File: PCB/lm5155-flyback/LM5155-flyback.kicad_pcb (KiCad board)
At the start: 2 copper layers, 49 x 35.5 mm, 36 parts, among them Q1 DMT6030LFCL-7, T1 EP7-5801_750315825, U1 LM5155

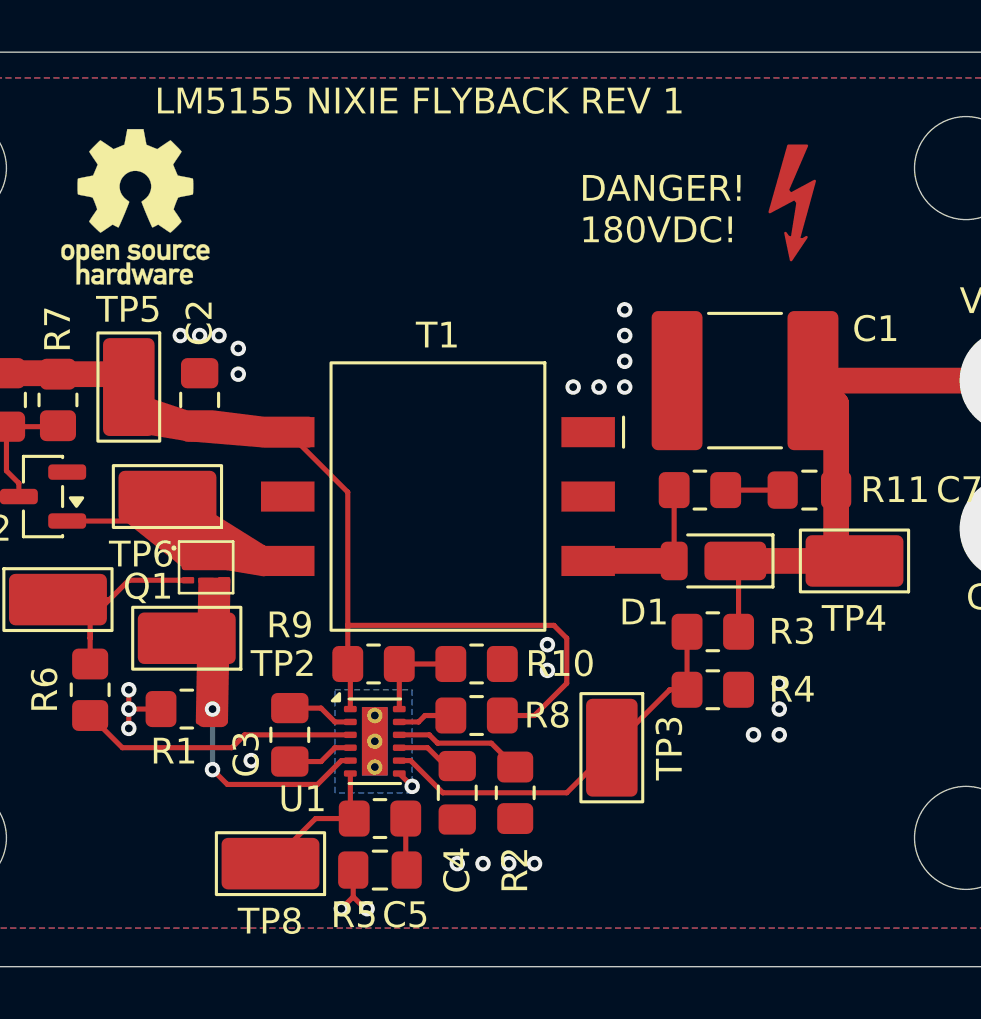
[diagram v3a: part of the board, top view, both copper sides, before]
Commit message: Fix small issue with feedback resistors. Hopefully wont cause real issues with Rev 1
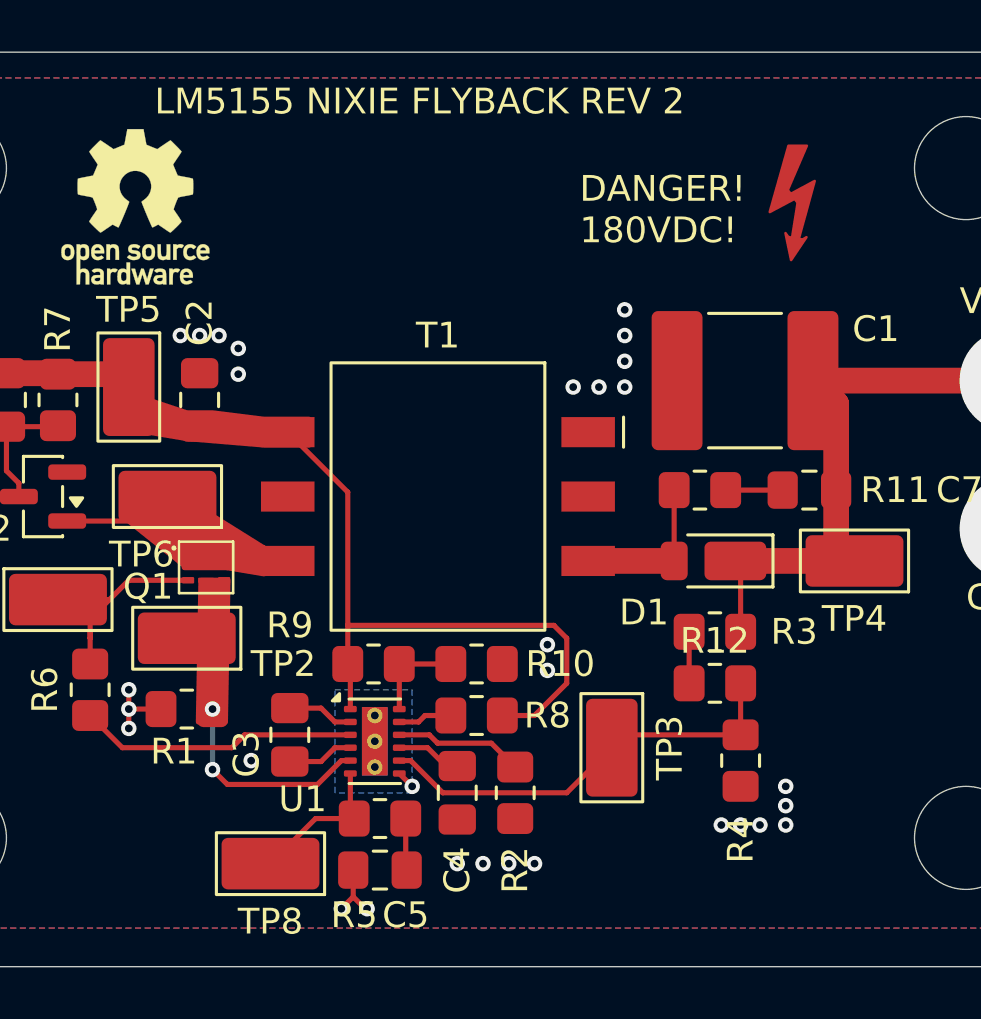
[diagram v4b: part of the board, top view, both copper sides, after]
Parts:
- added R12: 499k, Resistor_SMD:R_0805_2012Metric_Pad1.20x1.40mm_HandSolder, F.Cu at (191.5, 105.2)
- C4: value 30n -> 33n
- R2: value 87.5k -> 88.7k
- R3: value 1Meg -> 499k
- R7: value 3.8k -> 3.79k
- moved R4 2.95 mm to (192.5, 108.2), turned to -90 degrees
- moved R3 0.08 mm to (191.5, 103.2)
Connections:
- net Net-(D1-A) renamed /HV
- R3 pad 2: /FB -> Net-(R12-Pad1)
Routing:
- net Net-(R12-Pad1): track 0.00 -> 2.00 mm
- net /FB: track 15.6 -> 16.7 mm
- net GND: vias 30 -> 32
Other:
- board text added: "LM5155 NIXIE FLYBACK REV 2"
- board text removed: "LM5155 NIXIE FLYBACK REV 1"
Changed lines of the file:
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@@
 	(net 0 "")
 	(net 1 "unconnected-(T1-Pad2)")
-	(net 2 "Net-(D1-A)")
+	(net 2 "/HV")
 	(net 3 "/CS")
 	(net 4 "GND")
@@
 	(net 19 "/VOUT")
 	(net 20 "unconnected-(D2-NC-Pad2)")
+	(net 21 "Net-(R12-Pad1)")
 	(footprint "Symbol:Symbol_HighVoltage_NoTriangle_2x5mm_Copper"
 		(layer "F.Cu")
@@
 			)
 		)
-		(property "Value" "30n"
+		(property "Value" "33n"
 			(at 0 1.68 90)
 			(layer "F.Fab")
@@
 			)
 		)
-		(property "Value" "3.8k"
+		(property "Value" "3.79k"
 			(at 0 1.65 90)
 			(layer "F.Fab")
@@
 			(layers "F.Cu" "F.Mask" "F.Paste")
 			(roundrect_rratio 0.208333)
-			(net 2 "Net-(D1-A)")
+			(net 2 "/HV")
 			(pintype "passive")
 		)
@@
 			)
 		)
-		(property "Value" "87.5k"
+		(property "Value" "88.7k"
 			(at 0 1.65 90)
 			(layer "F.Fab")
@@
 	(footprint "Resistor_SMD:R_0805_2012Metric_Pad1.20x1.40mm_HandSolder"
 		(layer "F.Cu")
-		(at 191.42 103.25 180)
+		(at 191.5 103.25 180)
 		(descr "Resistor SMD 0805 (2012 Metric), square (rectangular) end terminal, IPC-7351 nominal with elongated pad for handsoldering. (Body size source: IPC-SM-782 page 72, https://www.pcb-3d.com/wordpress/wp-content/uploads/ipc-sm-782a_amendment_1_and_2.pdf), generated with kicad-footprint-generator")
 		(tags "resistor handsolder")
@@
 			)
 		)
-		(property "Value" "1Meg"
+		(property "Value" "499k"
 			(at 0 1.65 0)
 			(layer "F.Fab")
@@
 			(layers "F.Cu" "F.Mask" "F.Paste")
 			(roundrect_rratio 0.208333)
-			(net 12 "/FB")
+			(net 21 "Net-(R12-Pad1)")
 			(pintype "passive")
 		)
@@
 			(size 1.17 2.08)
 			(layers "F.Cu" "F.Mask" "F.Paste")
-			(net 2 "Net-(D1-A)")
+			(net 2 "/HV")
 			(pinfunction "3")
 			(pintype "passive")
@@
 	(footprint "Resistor_SMD:R_0805_2012Metric_Pad1.20x1.40mm_HandSolder"
 		(layer "F.Cu")
-		(at 191.42 105.5)
+		(at 192.5 108.25 -90)
 		(descr "Resistor SMD 0805 (2012 Metric), square (rectangular) end terminal, IPC-7351 nominal with elongated pad for handsoldering. (Body size source: IPC-SM-782 page 72, https://www.pcb-3d.com/wordpress/wp-content/uploads/ipc-sm-782a_amendment_1_and_2.pdf), generated with kicad-footprint-generator")
 		(tags "resistor handsolder")
 		(property "Reference" "R4"
-			(at 3.08 0 0)
+			(at 3.08 0 90)
 			(layer "F.SilkS")
 			(effects
@@
 		)
 		(property "Value" "5.6k"
+			(at 0 1.65 90)
+			(layer "F.Fab")
+			(effects
+				(font
+					(size 1 1)
+					(thickness 0.15)
+				)
+			)
+		)
+		(property "Datasheet" "~"
+			(at 0 0 90)
+			(layer "F.Fab")
+			(hide yes)
+			(effects
+				(font
+					(size 1.27 1.27)
+					(thickness 0.15)
+				)
+			)
+		)
+		(property "Description" "Resistor"
+			(at 0 0 90)
+			(layer "F.Fab")
+			(hide yes)
+			(effects
+				(font
+					(size 1.27 1.27)
+					(thickness 0.15)
+				)
+			)
+		)
+		(property ki_fp_filters "R_*")
+		(sheetname "/")
+		(sheetfile "LM5155-flyback.kicad_sch")
+		(attr smd)
+		(fp_line
+			(start -0.227064 0.735)
+			(end 0.227064 0.735)
+			(stroke
+				(width 0.12)
+				(type solid)
+			)
+			(layer "F.SilkS")
+		)
+		(fp_line
+			(start -0.227064 -0.735)
+			(end 0.227064 -0.735)
+			(stroke
+				(width 0.12)
+				(type solid)
+			)
+			(layer "F.SilkS")
+		)
+		(fp_rect
+			(start -1.85 -0.95)
+			(end 1.85 0.95)
+			(stroke
+				(width 0.05)
+				(type solid)
+			)
+			(fill no)
+			(layer "F.CrtYd")
+		)
+		(fp_rect
+			(start -1 -0.625)
+			(end 1 0.625)
+			(stroke
+				(width 0.1)
+				(type solid)
+			)
+			(fill no)
+			(layer "F.Fab")
+		)
+		(fp_text user "${REFERENCE}"
+			(at 0 0 90)
+			(layer "F.Fab")
+			(effects
+				(font
+					(size 0.5 0.5)
+					(thickness 0.08)
+				)
+			)
+		)
+		(pad "1" smd roundrect
+			(at -1 0 270)
+			(size 1.2 1.4)
+			(layers "F.Cu" "F.Mask" "F.Paste")
+			(roundrect_rratio 0.208333)
+			(net 12 "/FB")
+			(pintype "passive")
+		)
+		(pad "2" smd roundrect
+			(at 1 0 270)
+			(size 1.2 1.4)
+			(layers "F.Cu" "F.Mask" "F.Paste")
+			(roundrect_rratio 0.208333)
+			(net 4 "GND")
+			(pintype "passive")
+		)
+		(embedded_fonts no)
+		(model "${KICAD9_3DMODEL_DIR}/Resistor_SMD.3dshapes/R_0805_2012Metric.step"
+			(offset
+				(xyz 0 0 0)
+			)
+			(scale
+				(xyz 1 1 1)
+			)
+			(rotate
+				(xyz 0 0 0)
+			)
+		)
+	)
+	(footprint "Resistor_SMD:R_0805_2012Metric_Pad1.20x1.40mm_HandSolder"
+		(layer "F.Cu")
+		(at 191.5 105.25)
+		(descr "Resistor SMD 0805 (2012 Metric), square (rectangular) end terminal, IPC-7351 nominal with elongated pad for handsoldering. (Body size source: IPC-SM-782 page 72, https://www.pcb-3d.com/wordpress/wp-content/uploads/ipc-sm-782a_amendment_1_and_2.pdf), generated with kicad-footprint-generator")
+		(tags "resistor handsolder")
+		(property "Reference" "R12"
+			(at 0 -1.65 0)
+			(layer "F.SilkS")
+			(effects
+				(font
+					(size 1 1)
+					(thickness 0.15)
+				)
+			)
+		)
+		(property "Value" "499k"
 			(at 0 1.65 0)
 			(layer "F.Fab")
@@
 			(layers "F.Cu" "F.Mask" "F.Paste")
 			(roundrect_rratio 0.208333)
-			(net 12 "/FB")
+			(net 21 "Net-(R12-Pad1)")
 			(pintype "passive")
 		)
@@
 			(layers "F.Cu" "F.Mask" "F.Paste")
 			(roundrect_rratio 0.208333)
-			(net 4 "GND")
+			(net 12 "/FB")
 			(pintype "passive")
 		)
@@
 			(layers "F.Cu" "F.Mask" "F.Paste")
 			(roundrect_rratio 0.2380952381)
-			(net 2 "Net-(D1-A)")
+			(net 2 "/HV")
 			(pinfunction "A")
 			(pintype "passive")
@@
 		)
 	)
-	(gr_text "LM5155 NIXIE FLYBACK REV 1"
+	(gr_text "LM5155 NIXIE FLYBACK REV 2"
 		(at 169.75 83.25 0)
 		(layer "F.SilkS")
@@
 	)
 	(via
+		(at 191.75 110.75)
+		(size 0.6)
+		(drill 0.3)
+		(layers "F.Cu" "B.Cu")
+		(free yes)
+		(net 4)
+	)
+	(via
 		(at 170.75 91.75)
 		(size 0.6)
@@
 	)
 	(via
+		(at 194.25 109.25)
+		(size 0.6)
+		(drill 0.3)
+		(layers "F.Cu" "B.Cu")
+		(free yes)
+		(net 4)
+	)
+	(via
 		(at 188 90.75)
 		(size 0.6)
@@
 	)
 	(via
-		(at 194 105.25)
+		(at 193.25 110.75)
 		(size 0.6)
 		(drill 0.3)
@@
 	)
 	(via
-		(at 194 107.25)
+		(at 194.25 110.75)
 		(size 0.6)
 		(drill 0.3)
@@
 	)
 	(via
+		(at 194.25 110)
+		(size 0.6)
+		(drill 0.3)
+		(layers "F.Cu" "B.Cu")
+		(free yes)
+		(net 4)
+	)
+	(via
 		(at 184.5 112.25)
 		(size 0.6)
@@
 	)
 	(via
-		(at 173.5 108.25)
+		(at 192.5 110.75)
 		(size 0.6)
 		(drill 0.3)
@@
 	)
 	(via
-		(at 177 114)
+		(at 173.5 108.25)
 		(size 0.6)
 		(drill 0.3)
@@
 	)
 	(via
-		(at 173 92.25)
+		(at 177 114)
 		(size 0.6)
 		(drill 0.3)
@@
 	)
 	(via
-		(at 168.75 107)
+		(at 173 92.25)
 		(size 0.6)
 		(drill 0.3)
@@
 	)
 	(via
-		(at 194 106.25)
+		(at 168.75 107)
 		(size 0.6)
 		(drill 0.3)
@@
 	)
 	(via
-		(at 193 107.25)
-		(size 0.6)
-		(drill 0.3)
-		(layers "F.Cu" "B.Cu")
-		(free yes)
-		(net 4)
-	)
-	(via
 		(at 179.75 109.25)
 		(size 0.6)
@@
 	)
 	(segment
-		(start 189.75 105.5)
-		(end 190.42 105.5)
+		(start 188 107.25)
+		(end 187.5 107.75)
 		(width 0.2)
 		(layer "F.Cu")
@@
 	)
 	(segment
-		(start 185.75 109.5)
-		(end 187.5 107.75)
+		(start 192.5 105.25)
+		(end 192.5 107.25)
 		(width 0.2)
 		(layer "F.Cu")
@@
 	)
 	(segment
-		(start 179.25 108.25)
-		(end 179.68884 108.25)
+		(start 185.75 109.5)
+		(end 187.5 107.75)
 		(width 0.2)
 		(layer "F.Cu")
@@
 	)
 	(segment
-		(start 190.42 103.25)
-		(end 190.42 105.5)
+		(start 192.5 107.25)
+		(end 188 107.25)
 		(width 0.2)
 		(layer "F.Cu")
@@
 	)
 	(segment
-		(start 187.5 107.75)
-		(end 189.75 105.5)
+		(start 179.25 108.25)
+		(end 179.68884 108.25)
 		(width 0.2)
 		(layer "F.Cu")
@@
 	)
 	(segment
-		(start 192.42 103.25)
-		(end 192.42 100.625)
+		(start 196.2075 94.4)
+		(end 196.2075 97.75)
+		(width 1)
+		(layer "F.Cu")
+		(net 19)
+	)
+	(segment
+		(start 192.5 103.25)
+		(end 192.5 100.705)
 		(width 0.2)
 		(layer "F.Cu")
@@
 	)
 	(segment
-		(start 196.2075 94.4)
-		(end 196.2075 97.75)
-		(width 1)
+		(start 192.5 100.705)
+		(end 192.295 100.5)
+		(width 0.2)
 		(layer "F.Cu")
 		(net 19)
@@
 		(net 19)
 	)
-	(segment
-		(start 192.42 100.625)
-		(end 192.295 100.5)
-		(width 0.2)
-		(layer "F.Cu")
-		(net 19)
-	)
 	(via
 		(at 203 93.5)
@@
 		(net 19)
 	)
+	(segment
+		(start 190.5 103.25)
+		(end 190.5 105.25)
+		(width 0.2)
+		(layer "F.Cu")
+		(net 21)
+	)
 	(zone

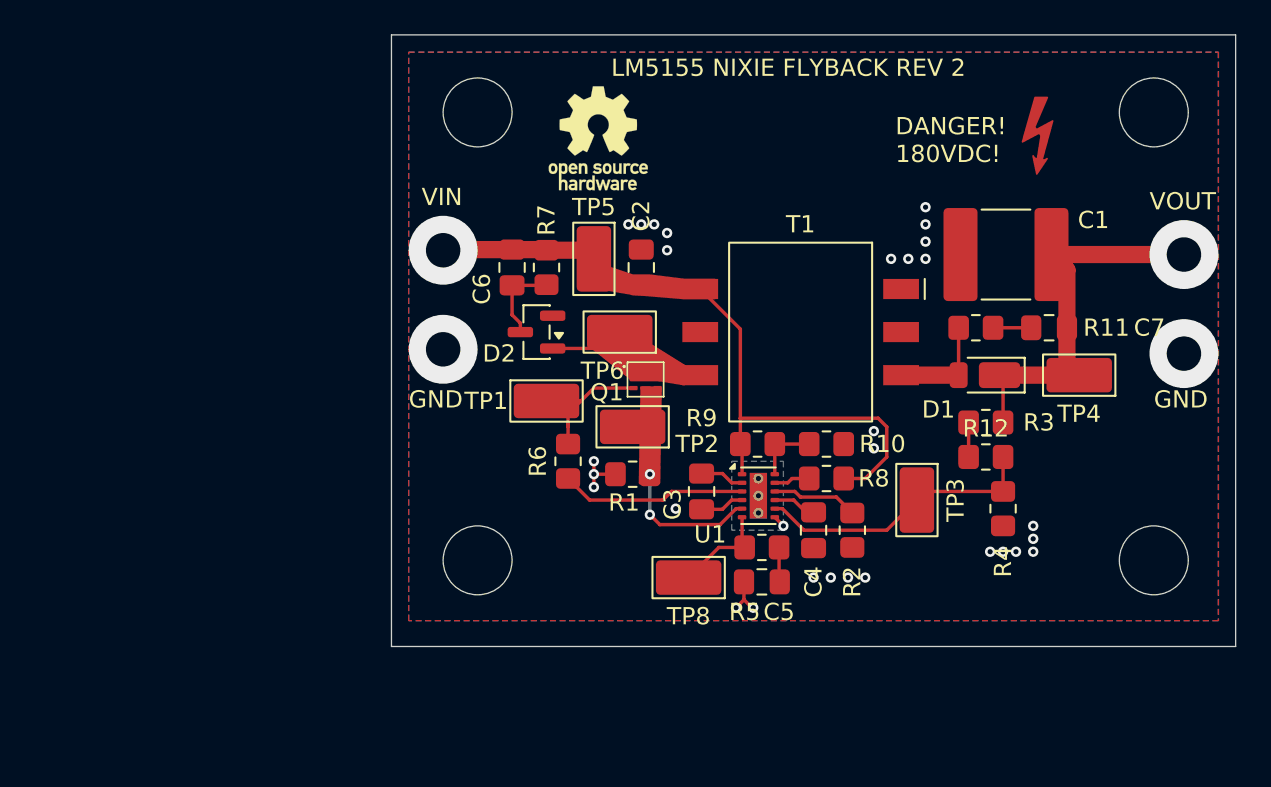
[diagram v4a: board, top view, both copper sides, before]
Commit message: Replaced LM5155 with LM5156H. Also replaced MOSFET. Packages just too difficult to solder.
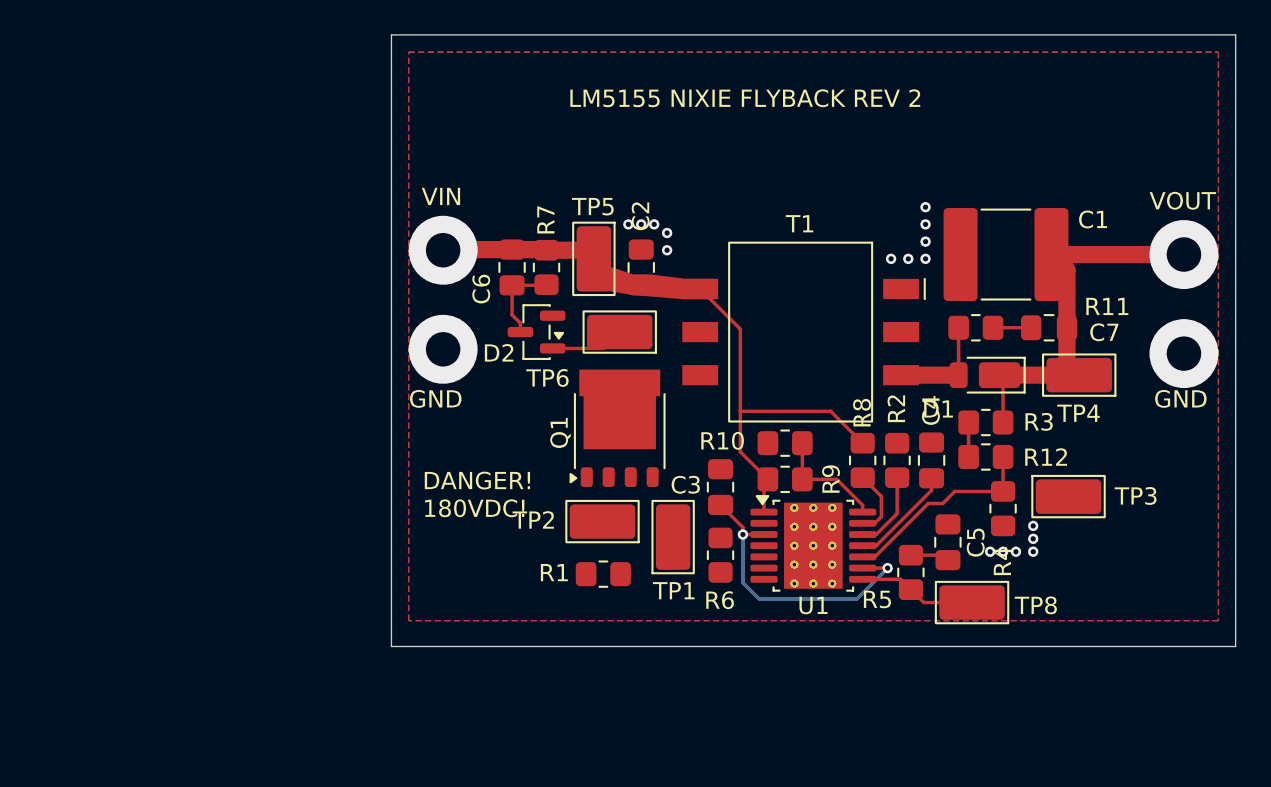
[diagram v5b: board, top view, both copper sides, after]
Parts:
- removed REF**: Symbol_HighVoltage_NoTriangle_2x5mm_Copper, Symbol:Symbol_HighVoltage_NoTriangle_2x5mm_Copper
- removed REF** (x4): MountingHole_4mm, MountingHole:MountingHole_4mm
- removed REF**: OSHW-Logo_5.7x6mm_SilkScreen, Symbol:OSHW-Logo_5.7x6mm_SilkScreen
- Q1: value DMT6030LFCL-7 -> PSMN014-80YL; footprint LM5155-flyback:U-DFN1616-6 -> Package_TO_SOT_SMD:LFPAK56
- U1: value LM5155 -> LM5156H; footprint LM5155-flyback:WSON-12-1EP_3x2mm_P0.5mm_EP1x2.65_ThermalVias -> Package_SO:Texas_HTSSOP-14-1EP_4.4x5mm_P0.65mm_EP3.4x5mm_Mask3.155x3.255mm_ThermalVias
- moved TP8 16.5 mm to (190.7, 113.7)
- moved C5 11.0 mm to (189.3, 110.2), turned to 90 degrees
- moved TP1 10.8 mm to (173.3, 109.9), turned to 90 degrees
- moved R6 10.4 mm to (176.1, 111.0), turned to -90 degrees
- moved TP3 8.80 mm to (196.3, 107.5), turned to 0 degrees
- moved R5 8.77 mm to (187.2, 112.0), turned to 90 degrees
- moved C4 7.96 mm to (188.3, 105.5), turned to 90 degrees
- moved R1 6.04 mm to (169.3, 112.0)
- moved TP2 5.77 mm to (169.2, 109.0)
- moved R2 4.81 mm to (186.3, 105.5), turned to -90 degrees
- moved U1 4.31 mm to (181.5, 110.4)
- moved Q1 3.35 mm to (170.2, 103.8), turned to 90 degrees
- moved R9 2.60 mm to (179.8, 106.5)
- moved R10 2.40 mm to (179.8, 104.5), turned to 180 degrees
- moved R8 2.35 mm to (184.3, 105.5), turned to -90 degrees
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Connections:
- C3 pad 2: Net-(U1-VCC) -> Net-(U1-DITHOFF)
- Q1 pad 1: /SW -> /CS
- Q1 pad 2: /GATE -> /CS
- U1 pad 10: /RT -> /FB
- U1 pad 11: /PGOOD -> /SS
- U1 pad 12: /UVLO -> /RT
- U1 pad 13: GND -> /PGOOD
- U1 pad 2: Net-(U1-VCC) -> unconnected-(U1-NC-Pad2)
- U1 pad 3: Net-(U1-GATE) -> Net-(U1-DITHOFF)
- U1 pad 4: GND -> Net-(U1-GATE)
- U1 pad 5: /CS -> GND
- U1 pad 6: /COMP -> GND
- U1 pad 7: GND -> /CS
- U1 pad 8: /FB -> /COMP
- U1 pad 9: /SS -> Net-(U1-DITHOFF)
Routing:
- net Net-(U1-DITHOFF): track 0.00 -> 17.3 mm, vias 0 -> 2
- net Net-(U1-GATE): track 10.8 -> 0.00 mm
- net GND: track 8.45 -> 0.00 mm, vias 32 -> 19
- net /GATE: track 8.42 -> 0.00 mm
- net /CS: track 8.32 -> 0.00 mm, vias 2 -> 0
- net /FB: track 16.7 -> 12.1 mm
- net /SS: track 2.55 -> 6.03 mm
- net /UVLO: track 3.75 -> 6.62 mm
- net /VIN: track 34.2 -> 31.5 mm
- net Net-(U1-VCC): track 2.57 -> 0.00 mm
- net /PGOOD: track 2.10 -> 3.97 mm
- net /COMP: track 5.79 -> 6.91 mm

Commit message: Layout changes
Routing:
- net GND: track 0.00 -> 12.0 mm, vias 19 -> 27
- net /CS: track 0.00 -> 9.46 mm
- net /GATE: track 0.00 -> 7.57 mm
- net Net-(U1-GATE): track 0.00 -> 2.71 mm
- added copper zone on F.Cu, net /CS
- added copper zone on F.Cu, net /SW

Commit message: updates
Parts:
- added R13: 1Meg, Resistor_SMD:R_0805_2012Metric_Pad1.20x1.40mm_HandSolder, F.Cu at (194.5, 88.2)
- added R14: 1Meg, Resistor_SMD:R_0805_2012Metric_Pad1.20x1.40mm_HandSolder, F.Cu at (190.0, 88.2)
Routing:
- net GND: track 12.0 -> 17.7 mm
- net /VOUT: track 22.8 -> 28.2 mm
- net /FB: track 12.1 -> 16.1 mm
- net Net-(R13-Pad2): track 0.00 -> 2.50 mm
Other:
- board size 49 x 35.5 mm -> 49 x 31 mm
- board text added: "NIXIE FLYBACK REV 2"
- board text removed: "LM5155 NIXIE FLYBACK REV 2"
